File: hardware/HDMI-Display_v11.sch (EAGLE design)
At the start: 107 parts, among them IC1 TFP401A-PAD, IC2 24LC02B, IC3 IS31BL3506A-TTLS2, IC4 ATMEGA32U4-MU, IC5 LDO-TS1117CW-3V3, J20_1 JUMPER2-0402, J20_2 JUMPER2-0402, J30_1 JUMPER2-0402, J30_2 JUMPER2-0402, Q1 16MHz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

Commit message: updated schematics and layout
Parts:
- L3, L4: value Ferrit@1A -> BLM18PG221SH1D
- USB: value USB-MICRO -> USB-MICROB; device we-con:USB-MICRO -> we-con:USB-MICROB
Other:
- moved on the sheet: C10, D1, Q1, R13, R14

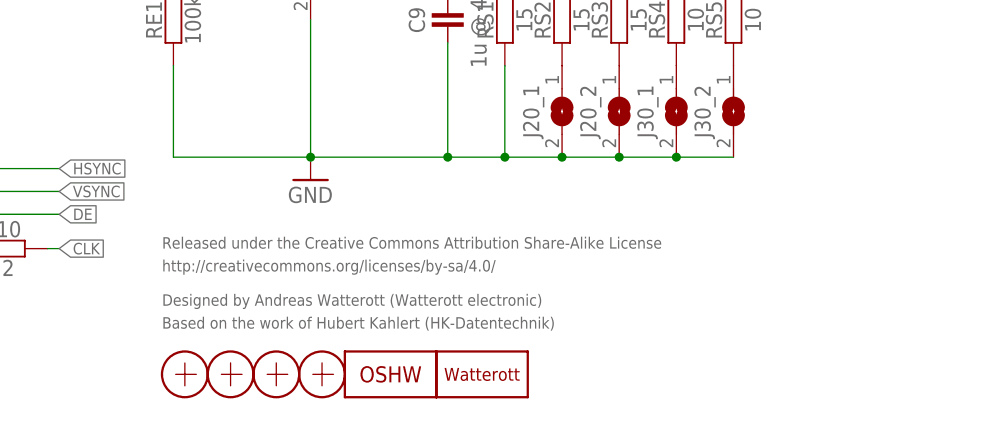
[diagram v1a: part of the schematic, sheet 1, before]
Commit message: updated schematics
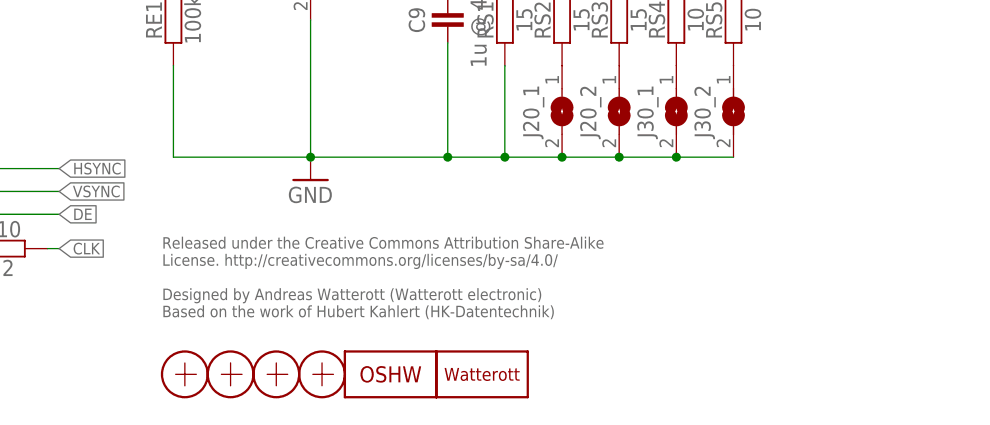
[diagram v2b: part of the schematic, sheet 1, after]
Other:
- note added: "Released under the Creative Commons Attribution Share-Alike License. http://creativecommons.org/licenses/by-sa/4.0/ Designed by Andreas Watterott (Watterott electronic) Based on the work of Hubert Kahlert (HK-Datentechnik)"
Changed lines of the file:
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@@
 <text x="224.79" y="57.15" size="1.778" layer="96" rot="R90">I = 0.3V / RS</text>
 <text x="179.07" y="71.755" size="1.27" layer="96" align="center">Digikey 490-5340-6-ND</text>
-<text x="162.56" y="21.59" size="1.27" layer="95">Released under the Creative Commons Attribution Share-Alike License</text>
-<text x="162.56" y="19.05" size="1.27" layer="95">http://creativecommons.org/licenses/by-sa/4.0/</text>
-<text x="162.56" y="15.24" size="1.27" layer="95">Designed by Andreas Watterott (Watterott electronic)</text>
-<text x="162.56" y="12.7" size="1.27" layer="95">Based on the work of Hubert Kahlert (HK-Datentechnik)</text>
+<text x="162.56" y="22.86" size="1.27" layer="95" align="top-left">Released under the Creative Commons Attribution Share-Alike
+License. http://creativecommons.org/licenses/by-sa/4.0/
+Designed by Andreas Watterott (Watterott electronic)
+Based on the work of Hubert Kahlert (HK-Datentechnik)</text>
 <text x="184.15" y="88.9" size="1.778" layer="97" rot="R90">TFT070-4 - 7" 800x480 BL:40mA
 TFT050-3 - 5" 800x480 BL:40mA
